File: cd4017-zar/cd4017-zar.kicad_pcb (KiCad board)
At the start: 2 copper layers, 47 parts, among them U1 NE555D, U2 4017

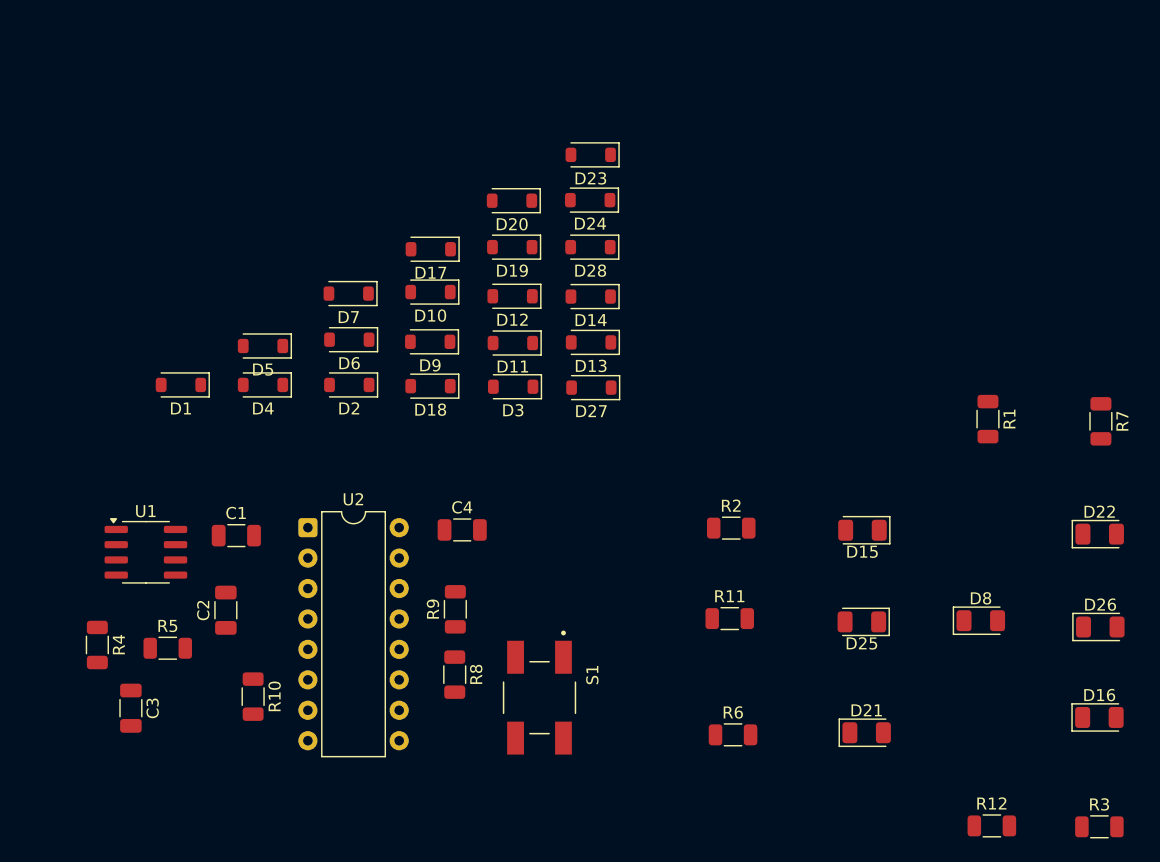
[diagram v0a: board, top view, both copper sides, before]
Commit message: zar footprint i eklendi
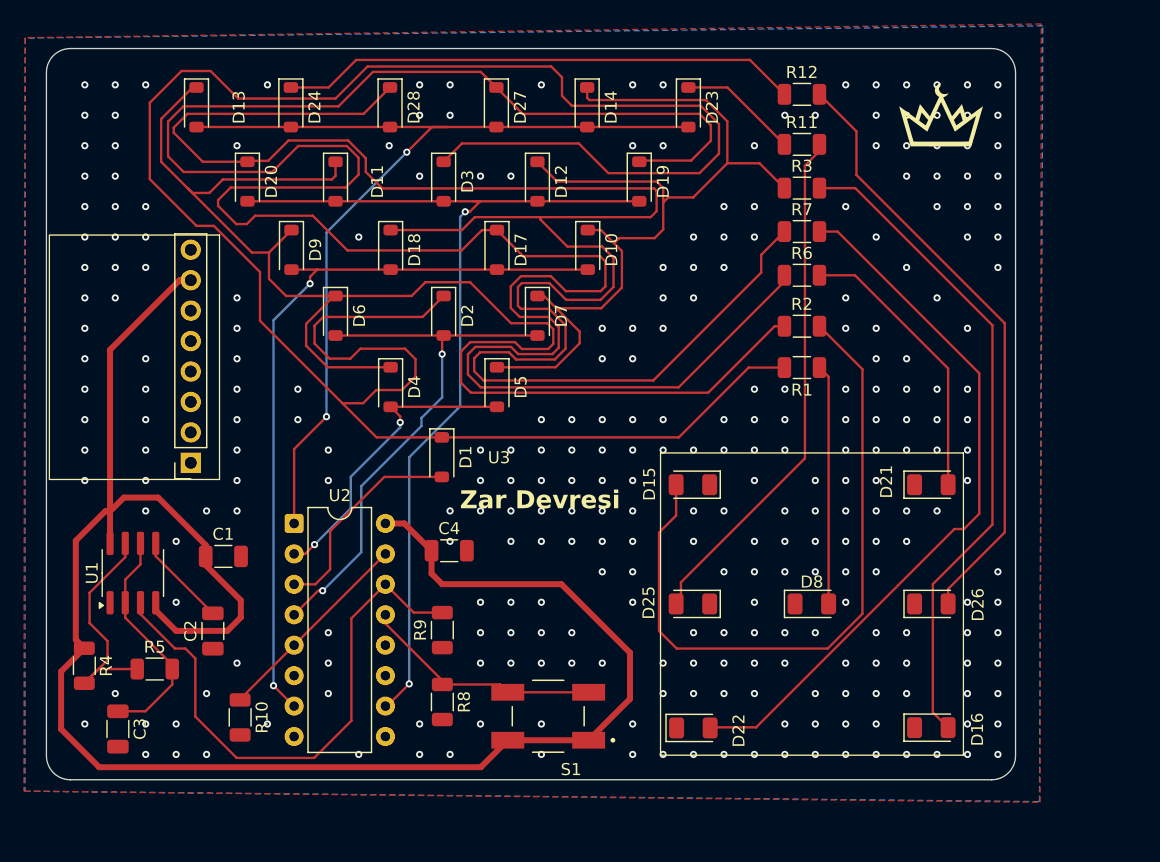
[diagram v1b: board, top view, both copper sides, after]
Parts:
- added G***: LOGO, tac:tac, F.Cu at (154.8, 27.2)
- added U3: ~, USB-C_Breakout:4090, F.Cu at (97.5, 46.9)
- moved R12 63.1 mm to (143.3, 24.9)
- moved R3 58.8 mm to (143.3, 32.7)
- moved R11 40.0 mm to (143.3, 29.1)
- moved R6 38.8 mm to (143.3, 40.0)
- moved D13 38.3 mm to (92.8, 26.0), turned to -90 degrees
- moved D22 37.6 mm to (134.2, 77.8)
- moved R7 29.6 mm to (143.3, 36.4), turned to 0 degrees
- moved D24 26.1 mm to (100.6, 26.0), turned to -90 degrees
- moved D27 24.7 mm to (117.8, 26.0), turned to -90 degrees
- moved D1 22.6 mm to (113.2, 55.2), turned to -90 degrees
- moved D20 22.1 mm to (97.0, 32.2), turned to -90 degrees
- moved D21 21.4 mm to (154.1, 57.5)
- moved D28 20.4 mm to (108.9, 26.0), turned to -90 degrees
- moved D11 20.0 mm to (104.3, 32.2), turned to -90 degrees
- moved D5 19.8 mm to (117.8, 49.3), turned to -90 degrees
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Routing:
- net Net-(D17-K): track 0.00 -> 188.5 mm
- net Net-(D1-K): track 0.00 -> 185.8 mm
- net Net-(D18-K): track 0.00 -> 158.0 mm
- net VCC: track 0.00 -> 153.3 mm
- net Net-(D11-K): track 0.00 -> 120.2 mm
- net ZAR_6: track 0.00 -> 80.2 mm, vias 0 -> 2
- net ZAR_5: track 0.00 -> 78.5 mm, vias 0 -> 2
- net Net-(D10-K): track 0.00 -> 74.8 mm
- net ZAR_4: track 0.00 -> 63.4 mm, vias 0 -> 2
- net Net-(D22-A): track 0.00 -> 59.8 mm
- net Net-(D15-A): track 0.00 -> 57.1 mm
- net Net-(D16-A): track 0.00 -> 55.3 mm
- net Net-(D26-A): track 0.00 -> 50.9 mm
- net TIMER: track 0.00 -> 45.9 mm
- net ZAR_3: track 0.00 -> 45.5 mm, vias 0 -> 2
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- added copper zone on B.Cu, net GND
- added copper zone on F.Cu, net GND
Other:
- board outline added: 80.9 x 61 mm
- board text added: "Zar Devresi"
